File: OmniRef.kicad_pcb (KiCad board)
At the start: 2 copper layers, 79.7 x 50.7 mm, 79 parts, among them J1 4mm Banana Jack Pair, J2 4mm Banana Jack Pair, Q1 PMBT3906, SW1 SW_SPDT, U1 REFERENCE IC, U2 LP2951, U3 REFERENCE IC

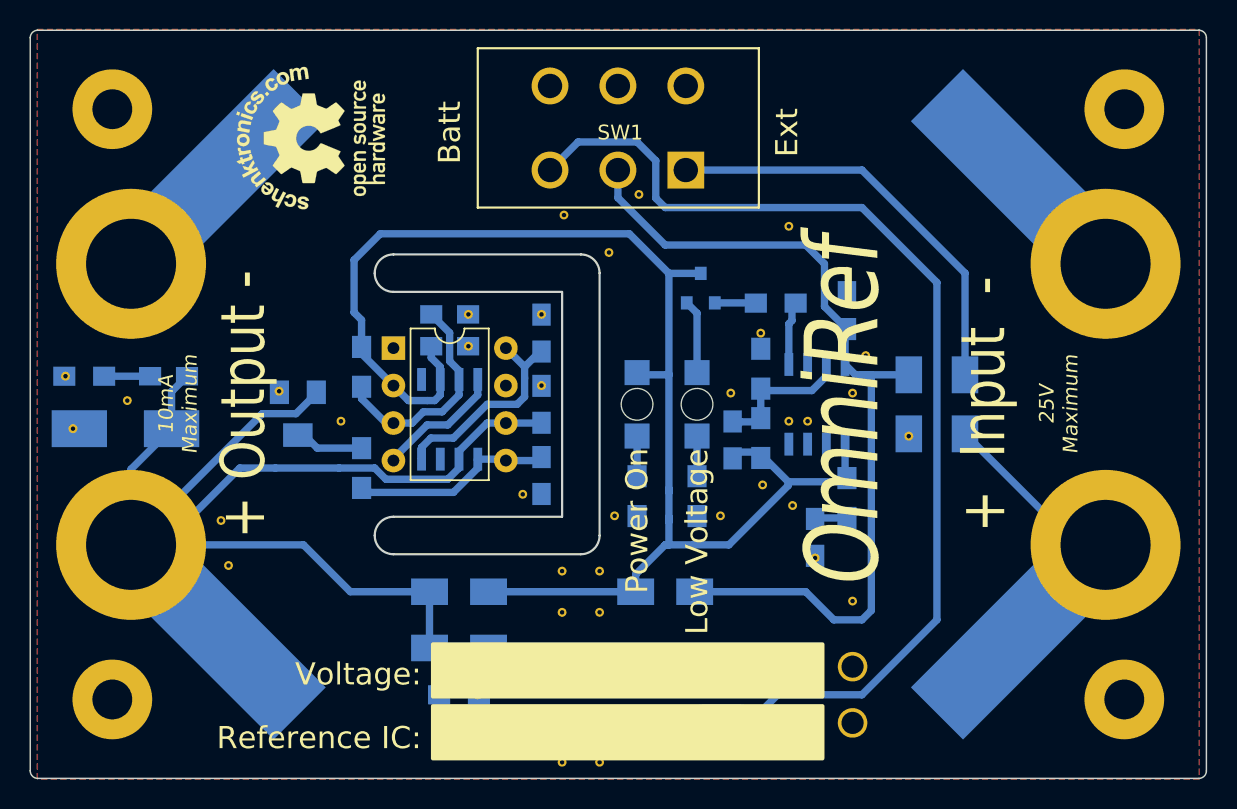
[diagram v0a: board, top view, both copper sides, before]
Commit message: Added DC-DC converter front end.  Adjusted some logos and stuff.
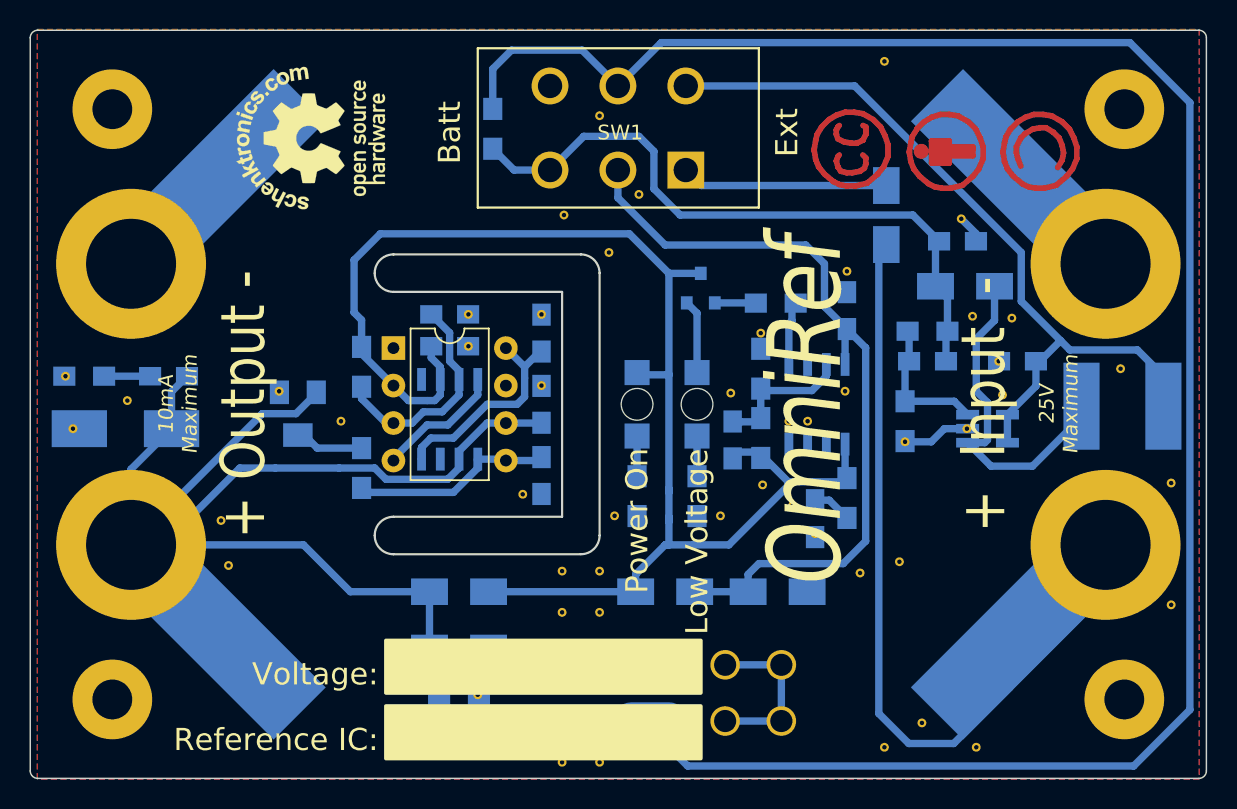
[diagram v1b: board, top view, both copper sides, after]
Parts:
- added C11: 10uF, Capacitors_SMD:C_0805_HandSoldering, B.Cu at (171.2, 80.3)
- added C12: 10pF, Capacitors_SMD:C_0805_HandSoldering, B.Cu at (165.1, 80.3)
- added C13: 10uF, Capacitors_SMD:C_0805_HandSoldering, B.Cu at (167.1, 72.1)
- added D8: D_Schottky, Diodes_SMD:D_SMA, B.Cu at (167.6, 75.2)
- added L1: L, Inductors:Inductor_Taiyo-Yuden_NR-60xx_HandSoldering, B.Cu at (178.3, 83.3)
- added R11: 0, Resistors_SMD:R_0805_HandSoldering, B.Cu at (135.6, 64.5)
- added R12: R, Resistors_SMD:R_0805_HandSoldering, B.Cu at (165.1, 78.2)
- added R13: R, Resistors_SMD:R_0805_HandSoldering, B.Cu at (163.6, 84.3)
- added REF**: 1pin, _NTSFootprints:Via_Tented_0.3mm, F.Cu at (167.4, 70.6)
- added REF**: 1pin, _NTSFootprints:Via_Tented_0.3mm, F.Cu at (178.2, 80.8)
- added REF**: 1pin, _NTSFootprints:Via_Tented_0.3mm, F.Cu at (170.2, 82.5)
- added REF**: 1pin, _NTSFootprints:Via_Tented_0.3mm, F.Cu at (170.8, 77.3)
- added REF**: 1pin, _NTSFootprints:Via_Tented_0.3mm, F.Cu at (169.9, 80.3)
- added REF**: 1pin, _NTSFootprints:Via_Tented_0.3mm, F.Cu at (168.1, 77.2)
- added REF**: 1pin, _NTSFootprints:Via_Tented_0.3mm, F.Cu at (142.9, 63.6)
- added REF**: 1pin, _NTSFootprints:Via_Tented_0.3mm, F.Cu at (181.6, 96.8)
- added REF**: 1pin, _NTSFootprints:Via_Tented_0.3mm, F.Cu at (168.4, 106.4)
- added REF**: Symbol_CC-ShareAlike_CopperTop_Small, Symbols:Symbol_CC-ShareAlike_CopperTop_Small, F.Cu at (172.7, 66.0)
- added REF**: Symbol_CC-Attribution_CopperTop_Small, Symbols:Symbol_CC-Attribution_CopperTop_Small, F.Cu at (166.4, 66.0)
- added REF**: Symbol_CreativeCommons_CopperTop_Type2_Small, Symbols:Symbol_CreativeCommons_CopperTop_Type2_Small, F.Cu at (160.0, 66.0)
- added REF**: 1pin, _NTSFootprints:Via_Tented_0.3mm, F.Cu at (162.2, 106.4)
- added REF**: 1pin, _NTSFootprints:Via_Tented_0.3mm, F.Cu at (163.2, 93.9)
- added REF**: 1pin, _NTSFootprints:Via_Tented_0.3mm, F.Cu at (164.7, 104.8)
- added REF**: 1pin, _NTSFootprints:Via_Tented_0.3mm, F.Cu at (181.6, 88.5)
- added U4: AP3015, TO_SOT_Packages_SMD:SOT-23-5_HandSoldering, B.Cu at (169.2, 84.8)
- SW1: value SW_SPDT -> SW_DPDT_x2
- moved D4 15.5 mm to (154.9, 95.9), turned to 0 degrees
- moved D1 13.9 mm to (162.3, 70.4)
- moved REF** 12.9 mm to (162.2, 59.9)
- moved REF** 8.46 mm to (167.8, 84.8)
- moved BT1 4.83 mm to (146.3, 104.6)
- moved REF** 1.97 mm to (160.5, 94.6)
- moved REF** 1.65 mm to (157.5, 91.9)
- moved C6 1.27 mm to (157.5, 90.9)
- moved REF** 0.52 mm to (159.5, 82.3)
- moved REF** 0.46 mm to (163.6, 85.7)
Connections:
- BT1 pad 1: BAT+ -> Net-(BT1-Pad1)
- SW1 pad 4: GND -> Net-(C11-Pad1)
- SW1 pad 5: GND -> Net-(BT1-Pad1)
- SW1 pad 6: GND -> (no net)
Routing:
- net Net-(BT1-Pad1): track 0.00 -> 135.3 mm
- net Net-(C11-Pad1): track 0.00 -> 53.1 mm
- net Net-(D1-Pad2): track 21.8 -> 55.6 mm
- net BAT+: track 72.8 -> 44.8 mm
- net Net-(D8-Pad2): track 0.00 -> 23.2 mm
- net GND: track 8.68 -> 26.6 mm
- net Net-(D1-Pad1): track 29.6 -> 14.9 mm
- net Net-(C12-Pad2): track 0.00 -> 9.52 mm
- net Net-(C2-Pad1): track 59.8 -> 53.9 mm

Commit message: Adjusted size of outline to improve board fit.
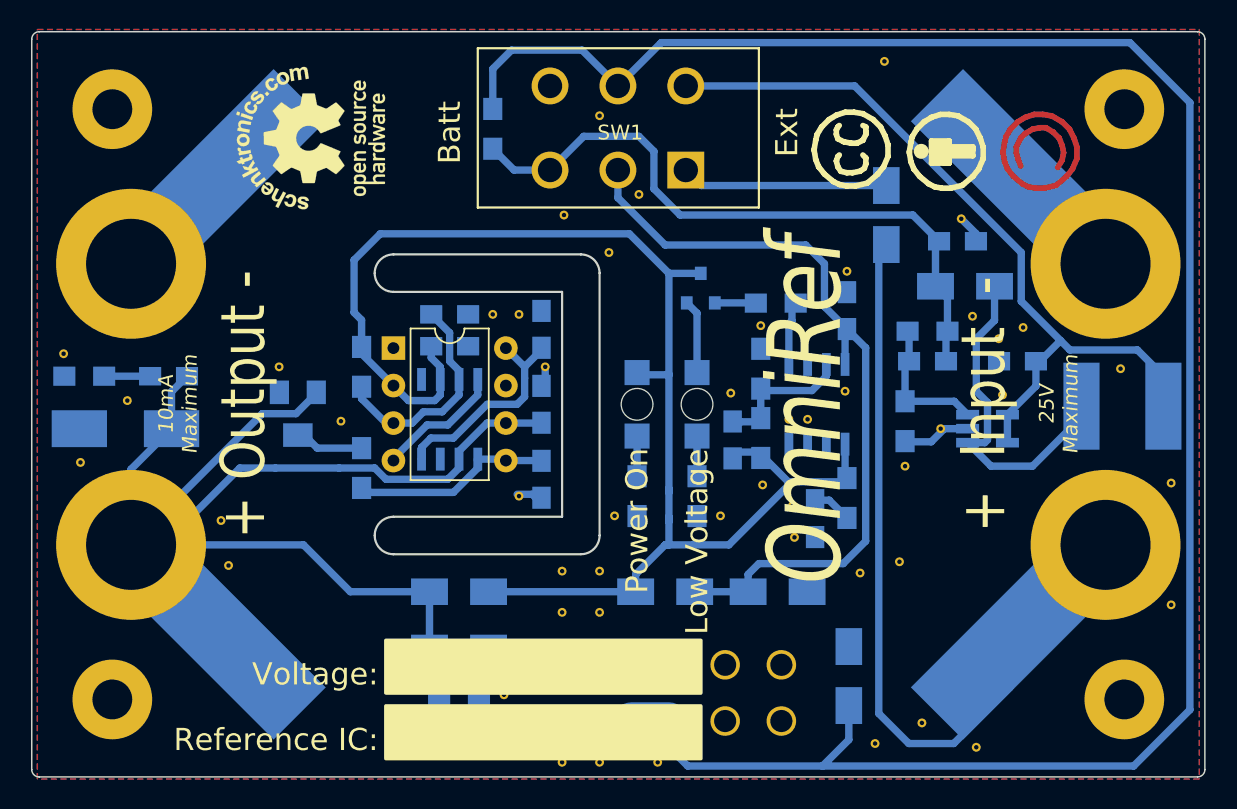
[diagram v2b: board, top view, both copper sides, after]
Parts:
- added D9: SMA, Diodes_SMD:D_SMA, B.Cu at (159.8, 101.6)
- REF**: footprint Symbols:Symbol_CreativeCommons_CopperTop_Type2_Small -> _NTSFootprints:Symbol_CreativeCommons_CopperTop_Type2_Small
- REF**: footprint Symbols:Symbol_CC-Attribution_CopperTop_Small -> _NTSFootprints:Symbol_CC-Attribution_SilkTop_Small
- moved REF** 31.0 mm to (146.8, 107.4)
- moved REF** 2.34 mm to (107.7, 87.1)
- moved REF** 2.29 mm to (137.5, 99.7)
- moved REF** 1.78 mm to (166.0, 84.8)
- moved REF** 1.78 mm to (136.4, 102.9)
- moved REF** 1.65 mm to (121.2, 80.6)
- moved REF** 1.65 mm to (163.6, 87.4)
- moved REF** 1.65 mm to (135.6, 77.1)
- moved REF** 1.53 mm to (106.6, 79.8)
- moved REF** 1.52 mm to (169.9, 78.7)
- moved REF** 1.52 mm to (137.4, 77.1)
- moved REF** 1.42 mm to (156.1, 92.2)
- moved REF** 1.30 mm to (139.2, 80.6)
- moved REF** 0.99 mm to (171.6, 78.0)
- moved REF** 0.68 mm to (161.5, 106.2)
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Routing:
- net GND: track 26.6 -> 18.3 mm
- net Net-(BT1-Pad1): track 135.3 -> 140.1 mm
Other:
- board size 79.7 x 50.7 mm -> 79.5 x 50.5 mm
